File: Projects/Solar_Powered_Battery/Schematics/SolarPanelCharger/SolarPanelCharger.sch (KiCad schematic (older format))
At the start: 0 parts

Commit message: update solar panel schematic
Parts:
- added C1, C2: 100n, Capacitor_SMD:C_0603_1608Metric_Pad1.05x0.95mm_HandSolder, symbol Device:C
- added D1, D2: SS14, custom-footprints:SMA_DO-214AC, symbol Device:D_Schottky
- added Q1, Q2: BC847, Package_TO_SOT_SMD:SOT-23, symbol Transistor_BJT:BC847
- added R1, R2: 51k, Resistor_SMD:R_0603_1608Metric_Pad1.05x0.95mm_HandSolder, symbol Device:R
- added R10, R5, R8: 10k, Resistor_SMD:R_0603_1608Metric_Pad1.05x0.95mm_HandSolder, symbol Device:R
- added R3: 18k, Resistor_SMD:R_0603_1608Metric_Pad1.05x0.95mm_HandSolder, symbol Device:R
- added R4, R9: 100k, Resistor_SMD:R_0603_1608Metric_Pad1.05x0.95mm_HandSolder, symbol Device:R
- added R6: 100, Resistor_SMD:R_0603_1608Metric_Pad1.05x0.95mm_HandSolder, symbol Device:R
- added R7: 47k, Resistor_SMD:R_0603_1608Metric_Pad1.05x0.95mm_HandSolder, symbol Device:R
- added U1: LM358, Package_SO:SOP-8_3.76x4.96mm_P1.27mm, symbol Amplifier_Operational:LM358
- added U2: TL431DBZ, Package_TO_SOT_SMD:SOT-23, symbol Reference_Voltage:TL431DBZ
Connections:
- net Buck_5V0/BUCK_IN: now also D1.2 (A), R1.1
- new net: R1.2, R2.1, U1.2 (-)
- new net: R6.2, U1.1
- new net: U1.6 (-), U1.7
- new net: R3.2, R4.1, U2.2 (REF)
- new net: C2.1, D1.1 (K), D2.1 (K), R10.1, R5.1, R8.1
- new net: Q1.1 (B), R6.1, R7.1
- new net: Q2.1 (B), R9.2
- new net BAT: C1.1, D2.2 (A), U1.8 (V+)
- new net EN_BAT: Q2.3 (C), R10.2
- new net GND: C1.2, C2.2, Q1.2 (E), Q2.2 (E), R2.2, R4.2, R7.2, U1.4 (V-), U1.5 (+), U2.3 (A)
- new net VREF_3V0: R3.1, R5.2, U1.3 (+), U2.1 (K)
- new net _EN_BAT: Q1.3 (C), R8.2, R9.1
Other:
- note added: "Switch to battery if the input voltage is below 6V"

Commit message: pcb updated
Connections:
- net LOGIC_SUPPLY: now reaches C2.1, D1.1 (K), D2.1 (K), R10.1, R5.1, R8.1
- net LOGIC_SUPPLY: now also C1.1, U1.8 (V+)
- removed net BAT: C1.1, D2.2 (A), U1.8 (V+)
- new net BOOST_5V0/BOOST_IN: D2.2 (A)
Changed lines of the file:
@@
 EESchema Schematic File Version 4
 LIBS:SolarPanelCharger-cache
-EELAYER 29 0
+EELAYER 26 0
 EELAYER END
 $Descr A4 11693 8268
@@
 Wire Wire Line
 	5050 6050 5050 6000
-Text Label 6200 2650 2    50   ~ 0
-BAT
 Text Label 5050 5900 2    50   ~ 0
-BAT
+LOGIC_SUPPLY
 $Comp
 L Device:C C1
@@
 	8150 3850 8150 4650
 Connection ~ 6850 3850
+Text Label 7200 3850 0    50   ~ 0
+LOGIC_SUPPLY
 $EndSCHEMATC

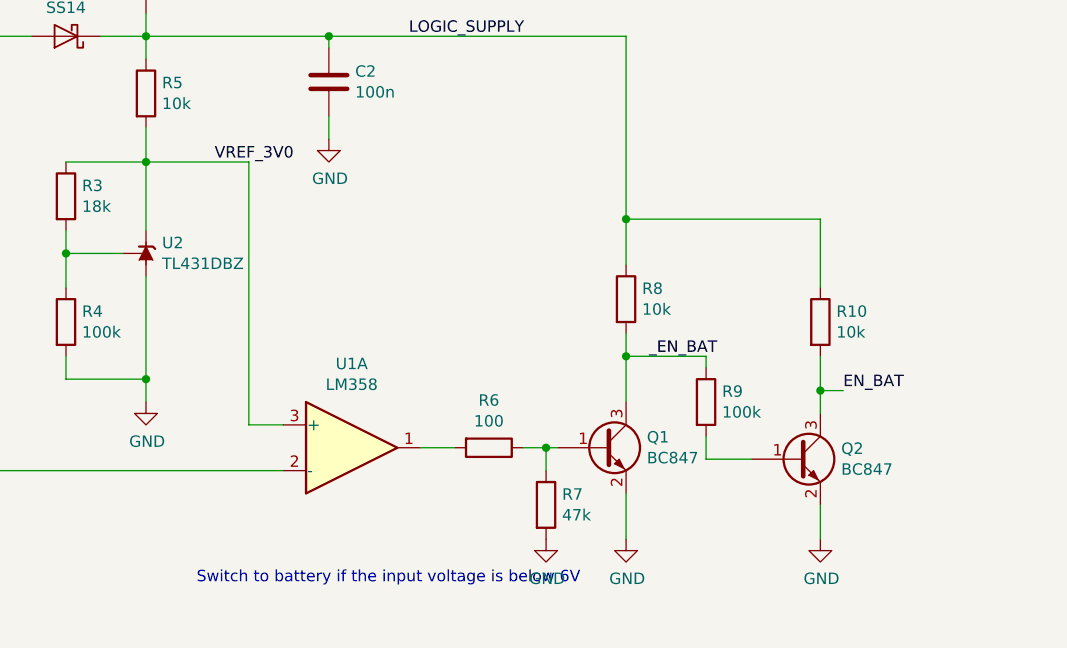
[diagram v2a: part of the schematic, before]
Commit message: make modifications to the solar charger circuit
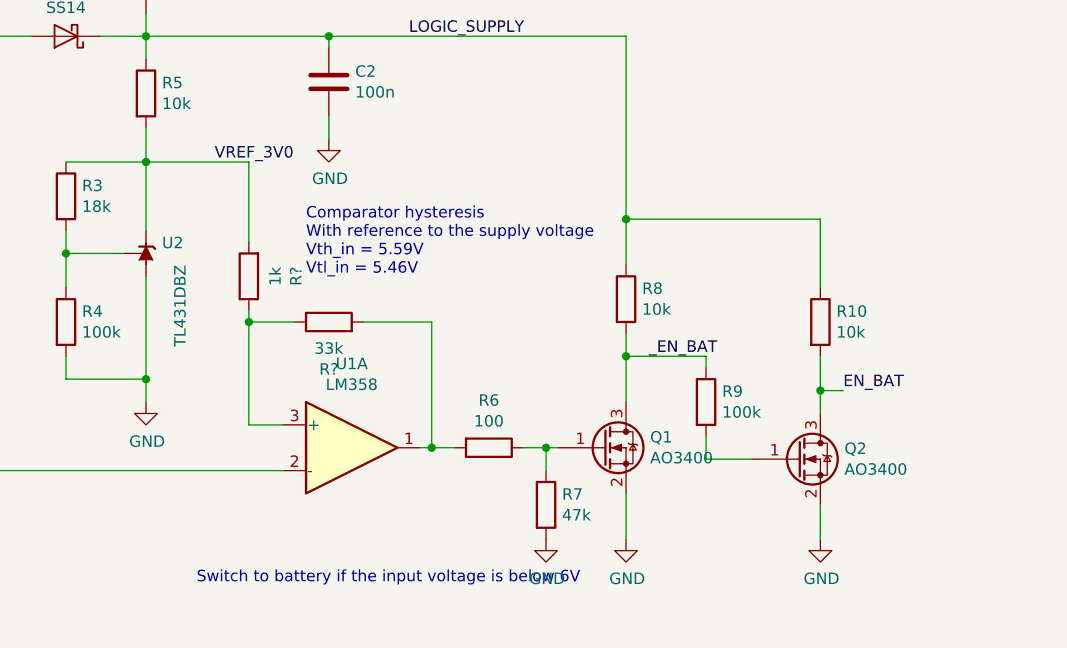
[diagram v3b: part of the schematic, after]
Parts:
- removed Q1, Q2: BC847, Package_TO_SOT_SMD:SOT-23, symbol Transistor_BJT:BC847
- added Q1, Q2: AO3400, symbol Device:Q_NMOS_GSD
- added R?: 1k, Resistor_SMD:R_0603_1608Metric_Pad1.05x0.95mm_HandSolder, symbol Device:R
- added R?: 33k, Resistor_SMD:R_0603_1608Metric_Pad1.05x0.95mm_HandSolder, symbol Device:R
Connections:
- net EN_BAT: now also Q2.3 (D)
- net GND: now also Q1.2 (S), Q2.2 (S)
- net VREF_3V0: now also R?.2; no longer U1.3 (+)
- net _EN_BAT: now also Q1.3 (D)
- net at R6.2, U1.1: now also R?.2
- net at R6.1, R7.1: now also Q1.1 (G)
- net at R9.2: now also Q2.1 (G)
- new net: R?.1, R?.1, U1.3 (+)
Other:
- note added: "Comparator hysteresis\nWith reference to the supply voltage\nVth_in = 5.59V\nVtl_in = 5.46V"
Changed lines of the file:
@@
 P 6050 4800
 F 0 "U2" V 6096 4730 50  0000 R CNN
-F 1 "TL431DBZ" V 6005 4730 50  0000 R CNN
+F 1 "TL431DBZ" H 6000 4650 50  0000 R CNN
 F 2 "Package_TO_SOT_SMD:SOT-23" H 6050 4650 50  0001 C CIN
 F 3 "http://www.ti.com/lit/ds/symlink/tl431.pdf" H 6050 4800 50  0001 C CIN
@@
 VREF_3V0
 Wire Wire Line
-	6500 4400 6500 5550
+	6500 4400 6500 4750
 Wire Wire Line
 	6500 5550 6650 5550
 Wire Wire Line
 	6050 4400 6500 4400
-$Comp
-L Transistor_BJT:BC847 Q1
-U 1 1 5CBBF64D
-P 8050 5650
-F 0 "Q1" H 8241 5696 50  0000 L CNN
-F 1 "BC847" H 8241 5605 50  0000 L CNN
-F 2 "Package_TO_SOT_SMD:SOT-23" H 8250 5575 50  0001 L CIN
-F 3 "http://www.infineon.com/dgdl/Infineon-BC847SERIES_BC848SERIES_BC849SERIES_BC850SERIES-DS-v01_01-en.pdf?fileId=db3a304314dca389011541d4630a1657" H 8050 5650 50  0001 L CNN
-	1    8050 5650
-	1    0    0    -1
-$EndComp
 $Comp
 L Device:R R6
@@
 $EndComp
 Wire Wire Line
-	7250 5650 7400 5650
+	7250 5650 7300 5650
 Wire Wire Line
 	7700 5650 7800 5650
@@
 F 3 "~" H 8500 5450 50  0001 C CNN
 	1    8500 5450
-	1    0    0    -1
-$EndComp
-$Comp
-L Transistor_BJT:BC847 Q2
-U 1 1 5CBC8521
-P 8900 5700
-F 0 "Q2" H 9091 5746 50  0000 L CNN
-F 1 "BC847" H 9091 5655 50  0000 L CNN
-F 2 "Package_TO_SOT_SMD:SOT-23" H 9100 5625 50  0001 L CIN
-F 3 "http://www.infineon.com/dgdl/Infineon-BC847SERIES_BC848SERIES_BC849SERIES_BC850SERIES-DS-v01_01-en.pdf?fileId=db3a304314dca389011541d4630a1657" H 8900 5700 50  0001 L CNN
-	1    8900 5700
 	1    0    0    -1
 $EndComp
@@
 Text Label 7200 3850 0    50   ~ 0
 LOGIC_SUPPLY
+$Comp
+L Device:Q_NMOS_GSD Q2
+U 1 1 5D1E2C62
+P 8900 5700
+F 0 "Q2" H 9105 5746 50  0000 L CNN
+F 1 "AO3400" H 9105 5655 50  0000 L CNN
+F 2 "" H 9100 5800 50  0001 C CNN
+F 3 "~" H 8900 5700 50  0001 C CNN
+	1    8900 5700
+	1    0    0    -1
+$EndComp
+$Comp
+L Device:Q_NMOS_GSD Q1
+U 1 1 5D1E2EDE
+P 8050 5650
+F 0 "Q1" H 8255 5696 50  0000 L CNN
+F 1 "AO3400" H 8255 5605 50  0000 L CNN
+F 2 "" H 8250 5750 50  0001 C CNN
+F 3 "~" H 8050 5650 50  0001 C CNN
+	1    8050 5650
+	1    0    0    -1
+$EndComp
+$Comp
+L Device:R R?
+U 1 1 5D1E4219
+P 6500 4900
+F 0 "R?" V 6293 4900 50  0000 C CNN
+F 1 "1k" V 6384 4900 50  0000 C CNN
+F 2 "Resistor_SMD:R_0603_1608Metric_Pad1.05x0.95mm_HandSolder" V 6430 4900 50  0001 C CNN
+F 3 "~" H 6500 4900 50  0001 C CNN
+	1    6500 4900
+	-1   0    0    1
+$EndComp
+Wire Wire Line
+	6500 5050 6500 5100
+$Comp
+L Device:R R?
+U 1 1 5D1E5A4B
+P 6850 5100
+F 0 "R?" V 6643 5100 50  0000 C CNN
+F 1 "33k" V 6734 5100 50  0000 C CNN
+F 2 "Resistor_SMD:R_0603_1608Metric_Pad1.05x0.95mm_HandSolder" V 6780 5100 50  0001 C CNN
+F 3 "~" H 6850 5100 50  0001 C CNN
+	1    6850 5100
+	0    -1   -1   0
+$EndComp
+Wire Wire Line
+	6500 5100 6700 5100
+Connection ~ 6500 5100
+Wire Wire Line
+	6500 5100 6500 5550
+Wire Wire Line
+	7000 5100 7300 5100
+Wire Wire Line
+	7300 5100 7300 5650
+Connection ~ 7300 5650
+Wire Wire Line
+	7300 5650 7400 5650
+Text Notes 6750 4900 0    50   ~ 0
+Comparator hysteresis\nWith reference to the supply voltage\nVth_in = 5.59V\nVtl_in = 5.46V
 $EndSCHEMATC
